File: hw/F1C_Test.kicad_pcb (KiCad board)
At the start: 2 copper layers, 0 parts

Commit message: hw: Partly done layout & routing
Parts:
- added C1: 22u, Capacitor_SMD:C_0603_1608Metric, F.Cu at (116.6, 59.5)
- added C10: 100n, Capacitor_SMD:C_0402_1005Metric, F.Cu at (139.1, 72.3)
- added C11: 100n, Capacitor_SMD:C_0402_1005Metric, F.Cu at (136.3, 74.3)
- added C12: 100n, Capacitor_SMD:C_0402_1005Metric, F.Cu at (132.9, 82.1)
- added C13: 10u, Capacitor_SMD:C_0402_1005Metric, F.Cu at (143.6, 85.6)
- added C14: 100n, Capacitor_SMD:C_0402_1005Metric, F.Cu at (144.3, 84.9)
- added C15: 100n, Capacitor_SMD:C_0402_1005Metric, F.Cu at (139.1, 88.0)
- added C16: 100n, Capacitor_SMD:C_0402_1005Metric, F.Cu at (145.1, 84.1)
- added C17: 100n, Capacitor_SMD:C_0402_1005Metric, F.Cu at (137.0, 73.6)
- added C18: 100n, Capacitor_SMD:C_0402_1005Metric, F.Cu at (134.6, 76.0)
- added C19: 100n, Capacitor_SMD:C_0402_1005Metric, F.Cu at (138.4, 70.0)
- added C2: 22u, Capacitor_SMD:C_0603_1608Metric, F.Cu at (122.6, 59.5)
- added C20: 4.7u, Capacitor_SMD:C_0402_1005Metric, F.Cu at (128.7, 86.2)
- added C21: 4.7u, Capacitor_SMD:C_0402_1005Metric, F.Cu at (128.4, 90.5)
- added C22: 10u, Capacitor_SMD:C_0402_1005Metric, F.Cu at (145.3, 62.6)
- added C23: 100n, Capacitor_SMD:C_0402_1005Metric, F.Cu at (119.5, 53.5)
- added C24: 100n, Capacitor_SMD:C_0402_1005Metric, F.Cu at (119.1, 65.2)
- added C25: 100n, Capacitor_SMD:C_0402_1005Metric, F.Cu at (121.0, 65.2)
- added C3: 22u, Capacitor_SMD:C_0603_1608Metric, F.Cu at (128.6, 59.5)
- added C4: 30p, Capacitor_SMD:C_0402_1005Metric, F.Cu at (150.3, 73.3)
- added C5: 30p, Capacitor_SMD:C_0402_1005Metric, F.Cu at (149.8, 77.6)
- added C6: 10u, Capacitor_SMD:C_0402_1005Metric, F.Cu at (132.1, 80.9)
- added C7: 100n, Capacitor_SMD:C_0402_1005Metric, F.Cu at (133.5, 82.8)
- added C8: 100n, Capacitor_SMD:C_0402_1005Metric, F.Cu at (137.8, 87.0)
- added C9: 100n, Capacitor_SMD:C_0402_1005Metric, F.Cu at (146.5, 77.4)
- added D1: 1N5819, Diode_SMD:D_SOD-323, F.Cu at (124.8, 88.2)
- added D2: White, LED_SMD:LED_0603_1608Metric, F.Cu at (150.6, 81.2)
- added J1: USB_C_Receptacle_USB2.0_14P, Connector_USB:USB_C_Receptacle_HRO_TYPE-C-31-M-12, F.Cu at (140.0, 51.7)
- added J2: FPC/FFC P0.5, FFC_Connector:FPC_1x40_P0.5_L, F.Cu at (140.0, 95.9)
- added J3: 1x03 P2.54, Connector_PinHeader_2.54mm:PinHeader_1x03_P2.54mm_Vertical, F.Cu at (156.4, 85.9)
- added J4: 1x06 P2.54, Connector_PinHeader_2.54mm:PinHeader_1x06_P2.54mm_Vertical, F.Cu at (156.4, 63.8)
- added J5: AudioJack4, Connector_Audio:Jack_3.5mm_KoreanHropartsElec_PJ-320D-4A_Horizontal, F.Cu at (122.7, 73.3)
- added L1: 4.7u, Inductor_SMD:L_Sunlord_SWPA3015S, F.Cu at (119.2, 59.8)
- added L2: 4.7u, Inductor_SMD:L_Sunlord_SWPA3015S, F.Cu at (125.2, 59.8)
- added L3: 2.2u, Inductor_SMD:L_Sunlord_SWPA3015S, F.Cu at (131.2, 59.8)
- added L4: 4.7u, Inductor_SMD:L_Sunlord_SWPA3015S, F.Cu at (125.9, 84.9)
- added R1: 560k, Resistor_SMD:R_0402_1005Metric, F.Cu at (116.8, 57.1)
- added R10: 4.7k, Resistor_SMD:R_0402_1005Metric, F.Cu at (148.2, 81.2)
- added R11: 4.7, Resistor_SMD:R_0402_1005Metric, F.Cu at (119.1, 67.2)
- added R12: 4.7, Resistor_SMD:R_0402_1005Metric, F.Cu at (121.0, 67.2)
- added R13: 5.1k, Resistor_SMD:R_0402_1005Metric, F.Cu at (140.6, 58.4)
- added R14: 5.1k, Resistor_SMD:R_0402_1005Metric, F.Cu at (138.6, 58.4)
- added R15: 100k, Resistor_SMD:R_0402_1005Metric, F.Cu at (153.8, 57.6)
- added R16: 100k, Resistor_SMD:R_0402_1005Metric, F.Cu at (162.4, 57.3)
- added R2: 130k, Resistor_SMD:R_0402_1005Metric, F.Cu at (116.8, 55.2)
- added R3: 110k, Resistor_SMD:R_0402_1005Metric, F.Cu at (122.8, 57.1)
- added R4: 33k, Resistor_SMD:R_0402_1005Metric, F.Cu at (122.8, 55.2)
- added R5: 110k, Resistor_SMD:R_0402_1005Metric, F.Cu at (128.8, 57.1)
- added R6: 130k, Resistor_SMD:R_0402_1005Metric, F.Cu at (128.8, 55.2)
- added R7: 2.2k, Resistor_SMD:R_0402_1005Metric, F.Cu at (145.0, 86.3)
- added R8: 2.2k, Resistor_SMD:R_0402_1005Metric, F.Cu at (146.3, 84.9)
- added R9: 4.7, Resistor_SMD:R_0402_1005Metric, F.Cu at (126.5, 90.5)
- added SW1: SW_Push, Button_Switch_SMD:SW_Push_1TS009xxxx-xxxx-xxxx_6x6x5mm, F.Cu at (153.2, 52.5)
- added SW2: SW_Push, Button_Switch_SMD:SW_Push_1TS009xxxx-xxxx-xxxx_6x6x5mm, F.Cu at (162.2, 52.3)
- added SW3: SW_SPST, Switches:SPST_1x01_P2.54, F.Cu at (140.1, 61.2)
- added U1: ME3103, Package_TO_SOT_SMD:SOT-23-5, F.Cu at (119.0, 56.0)
- added U2: ME3103, Package_TO_SOT_SMD:SOT-23-5, F.Cu at (125.0, 56.0)
- added U3: ME3103, Package_TO_SOT_SMD:SOT-23-5, F.Cu at (131.0, 56.0)
- added U4: F1C100s, F1C100s:QFN40P1000X1000X90-89N-D, F.Cu at (140.0, 80.0)
- added U5: W25Q32JVSS, Package_SO:SOIC-8_5.3x5.3mm_P1.27mm, F.Cu at (143.2, 70.0)
- added U6: MT9284, Package_TO_SOT_SMD:SOT-23-6, F.Cu at (127.8, 88.3)
- added Y1: 24MHz 20pF, Crystal:Crystal_SMD_3225-4Pin_3.2x2.5mm, F.Cu at (148.8, 75.5)
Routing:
- net /PWR: track 0.00 -> 29.1 mm
- net /LCD_VSYNC: track 0.00 -> 28.1 mm, vias 0 -> 2
- net /LCD_DE: track 0.00 -> 25.7 mm, vias 0 -> 2
- net /LCD_HSYNC: track 0.00 -> 25.3 mm, vias 0 -> 2
- net /LCD_PCLK: track 0.00 -> 24.6 mm, vias 0 -> 2
- net /JTAG_TCK: track 0.00 -> 16.3 mm
- net /LCD_D2: track 0.00 -> 15.9 mm
- net /LCD_D3: track 0.00 -> 15.7 mm
- net /LCD_D4: track 0.00 -> 15.6 mm
- net /LCD_D5: track 0.00 -> 15.4 mm
- net /LCD_D6: track 0.00 -> 15.3 mm
- net /LCD_D7: track 0.00 -> 15.1 mm
- net /LCD_D10: track 0.00 -> 14.9 mm
- net /LCD_D11: track 0.00 -> 14.8 mm
- net /LCD_D12: track 0.00 -> 14.6 mm
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- added copper zone on B.Cu, net GND
- added copper zone on F.Cu, net GND

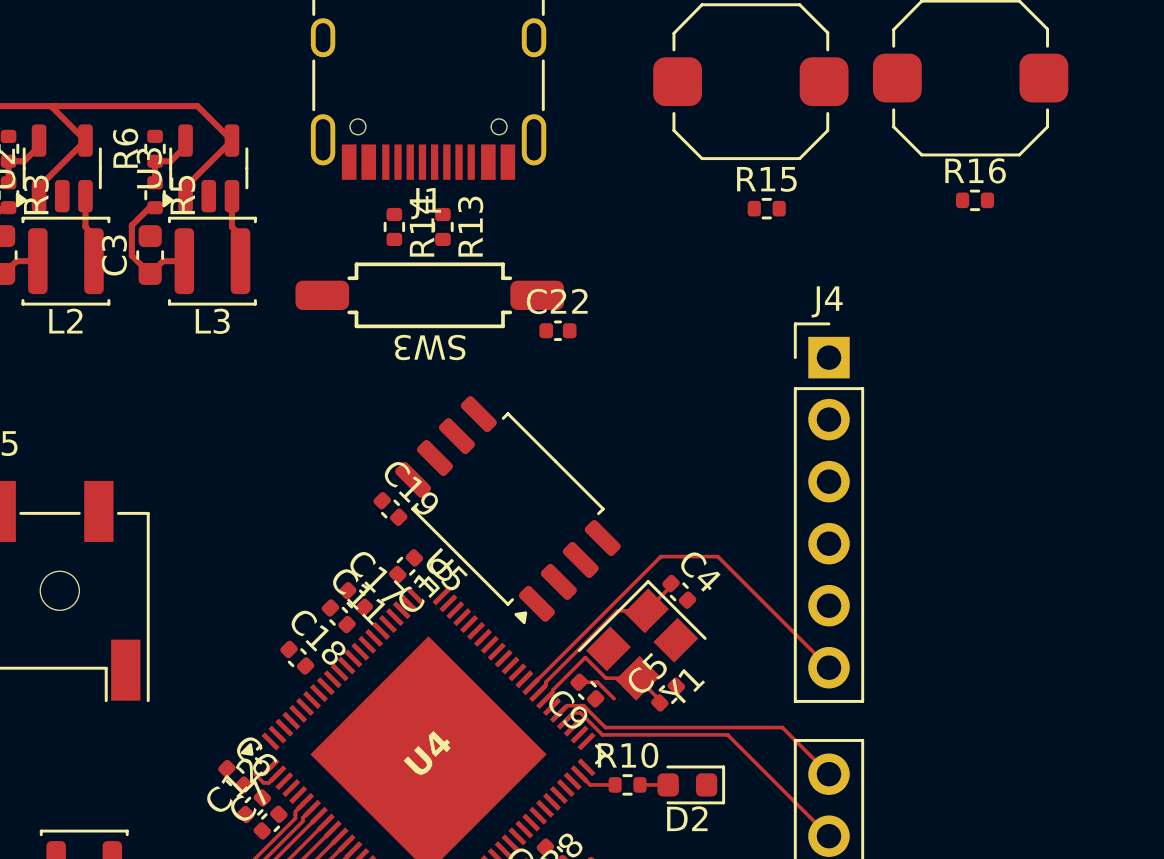
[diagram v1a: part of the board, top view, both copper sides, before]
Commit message: hw: Add VRA decoupling networks
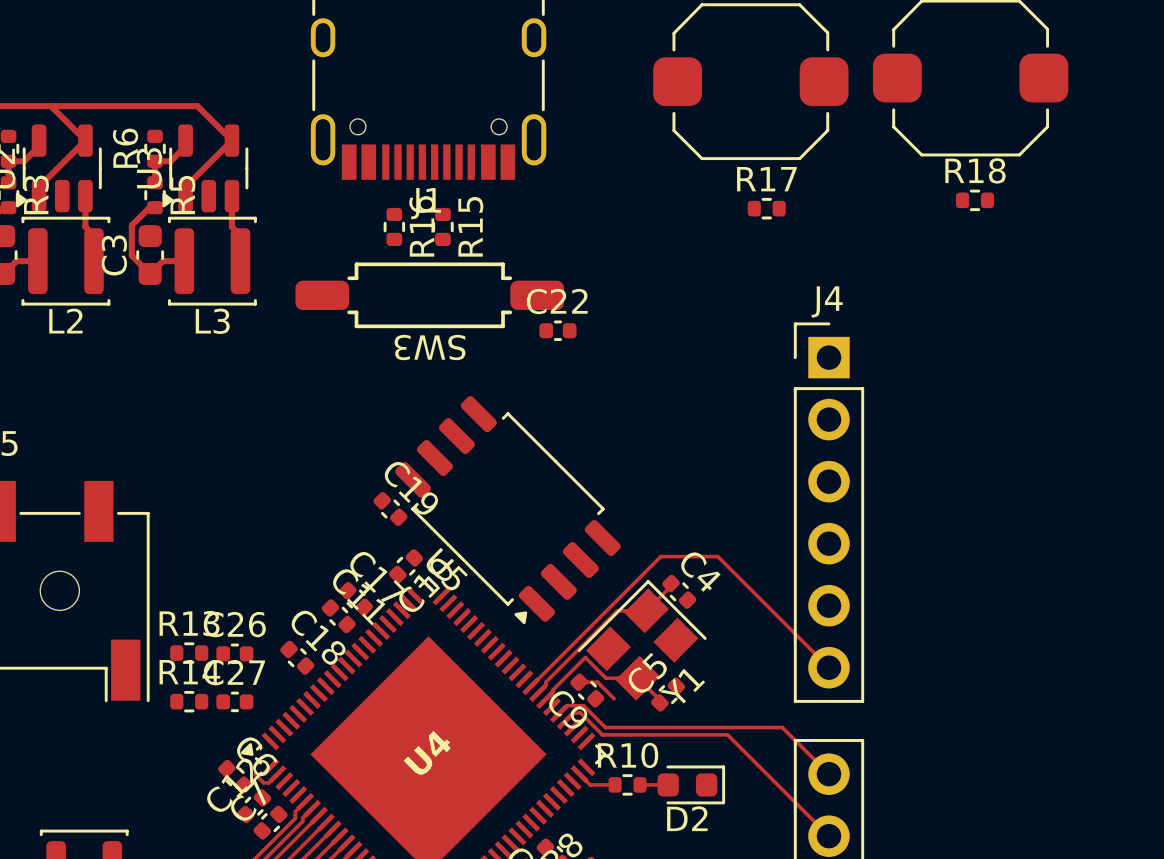
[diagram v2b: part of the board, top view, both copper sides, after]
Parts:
- added C26: 1u, Capacitor_SMD:C_0402_1005Metric, F.Cu at (132.1, 75.9)
- added C27: 1u, Capacitor_SMD:C_0402_1005Metric, F.Cu at (132.1, 77.8)
- added R13: 200k, Resistor_SMD:R_0402_1005Metric, F.Cu at (130.2, 75.8)
- added R14: 200k, Resistor_SMD:R_0402_1005Metric, F.Cu at (130.2, 77.8)
- renumbered R13 to R15, R14 to R16, R15 to R17, R16 to R18
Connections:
- U4 pad 81: unconnected-(U4A-VRA1-Pad81) -> /VRA1
- U4 pad 83: unconnected-(U4A-VRA2-Pad83) -> /VRA2

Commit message: hw: Further incomplete revisions...
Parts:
- J2: footprint FFC_Connector:FPC_1x40_P0.5_L -> FFC_Connector:FPC_1x40_P0.5_R
- moved D1 25.4 mm to (150.1, 90.2)
- moved R9 25.4 mm to (151.8, 92.5)
- moved U6 25.4 mm to (153.1, 90.3)
- moved C20 25.4 mm to (153.9, 88.1)
- moved C21 25.4 mm to (153.7, 92.5)
- moved L4 25.4 mm to (151.2, 86.8)
- moved C19 0.83 mm to (137.7, 69.6)
- moved U5 0.83 mm to (142.5, 69.6)
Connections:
- U4 pad 38: /LCD_NRST -> unconnected-(U4A-PE11/CLK_OUT/TWI0_SCK/IR_RX/EINTE11-Pad38)
- U4 pad 45: unconnected-(U4A-PE4/CSI_D1/LCD_D16/DA_LRCK/RSB_SDA/EINTE4-Pad45) -> /LCD_NRST
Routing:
- net /LCD_VSYNC: track 28.1 -> 6.73 mm, vias 2 -> 0
- net /LCD_DE: track 25.7 -> 6.72 mm, vias 2 -> 0
- net /LCD_HSYNC: track 25.3 -> 6.62 mm, vias 2 -> 0
- net /LCD_LED_DIM: track 0.00 -> 18.0 mm, vias 0 -> 2
- net /LCD_CS: track 0.00 -> 16.9 mm, vias 0 -> 2
- net /JTAG_TMS: track 0.00 -> 16.5 mm
- net /LCD_NRST: track 0.00 -> 16.3 mm
- net /JTAG_TDI: track 0.00 -> 16.0 mm
- net /JTAG_TDO: track 0.00 -> 15.8 mm
- net /LCD_MOSI: track 0.00 -> 14.7 mm
- net /LCD_PCLK: track 24.6 -> 9.87 mm, vias 2 -> 0
- net /LCD_SCLK: track 0.00 -> 14.5 mm
- net /FLASH_CLK: track 0.00 -> 12.7 mm
- net /FLASH_MOSI: track 0.00 -> 11.8 mm
- net /LCD_D19: track 13.9 -> 3.42 mm
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
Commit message: hw: Layout & routing (WIP)
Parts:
- moved R2 17.8 mm to (131.9, 45.8), turned to 0 degrees
- moved C1 17.8 mm to (127.5, 45.5), turned to 0 degrees
- moved R1 17.4 mm to (130.0, 45.8), turned to 180 degrees
- moved U1 14.5 mm to (131.1, 48.0), turned to 0 degrees
- moved L1 14.3 mm to (127.3, 48.1), turned to 90 degrees
- moved C23 14.0 mm to (133.2, 56.5)
- moved R18 13.7 mm to (149.4, 52.9)
- moved C24 13.2 mm to (127.0, 75.8), turned to 180 degrees
- moved R11 13.0 mm to (128.9, 75.8), turned to 180 degrees
- moved R17 11.8 mm to (146.1, 66.5)
- moved SW1 11.3 mm to (148.3, 62.7), turned to 90 degrees
- moved SW2 11.0 mm to (151.7, 49.0), turned to 90 degrees
- moved C25 10.4 mm to (127.0, 73.8), turned to 180 degrees
- moved R12 10.2 mm to (128.9, 73.8), turned to 180 degrees
- moved J5 9.92 mm to (130.7, 67.5)
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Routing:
- net /USB_D+: track 0.00 -> 23.9 mm
- net /USB_D-: track 0.00 -> 23.7 mm
- net /HP_COM: track 1.21 -> 21.9 mm
- net /LCD_D21: track 2.64 -> 18.2 mm, vias 0 -> 2
- net /LCD_D22: track 2.83 -> 18.3 mm, vias 0 -> 2
- net Net-(C24-Pad1): track 0.00 -> 15.4 mm
- net /LCD_D20: track 2.66 -> 16.2 mm, vias 0 -> 2
- net /LCD_D18: track 3.76 -> 16.6 mm, vias 0 -> 2
- net /LCD_D19: track 3.42 -> 16.2 mm, vias 0 -> 2
- net /LCD_D15: track 4.14 -> 16.9 mm, vias 0 -> 2
- net /LCD_D14: track 4.56 -> 17.3 mm, vias 0 -> 2
- net /LCD_D13: track 4.97 -> 17.6 mm, vias 0 -> 2
- net /LCD_D12: track 5.39 -> 17.9 mm, vias 0 -> 2
- net /LCD_D11: track 5.80 -> 18.2 mm, vias 0 -> 2
- net /LCD_D10: track 6.22 -> 18.6 mm, vias 0 -> 2
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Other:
- board outline added: 32 x 56 mm

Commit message: hw: More routing
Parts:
- moved C22 4.00 mm to (144.2, 55.6)
- moved R18 1.20 mm to (148.2, 52.9)
- moved SW2 1.20 mm to (150.5, 49.0)
- moved R16 0.35 mm to (138.1, 54.4)
- moved C15 0.30 mm to (138.8, 88.1), turned to 45 degrees
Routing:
- net +3V3: track 6.88 -> 94.4 mm, vias 0 -> 6
- net /PWR: track 30.6 -> 89.9 mm, vias 0 -> 2
- net +2V6: track 5.17 -> 46.6 mm, vias 0 -> 2
- net +1V1: track 5.17 -> 36.5 mm, vias 0 -> 2
- net /FLASH_CS: track 2.35 -> 28.8 mm, vias 0 -> 2
- net VBUS: track 0.00 -> 23.3 mm, vias 0 -> 2
- net /~{RESET}: track 0.00 -> 23.0 mm, vias 0 -> 2
- net Net-(U4B-SVREF): track 0.00 -> 4.01 mm
- net /USB_D+: track 23.9 -> 26.8 mm
- net /USB_D-: track 23.7 -> 26.0 mm, vias 0 -> 2
- net Net-(J1-CC2): track 0.00 -> 1.73 mm
- net Net-(J1-CC1): track 0.00 -> 1.73 mm
- net /LCD_D23: track 13.1 -> 12.6 mm
- net /LCD_D22: track 18.3 -> 17.8 mm
- net GND: vias 6 -> 15

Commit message: hw: Finish routing, finally
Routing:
- net +3V3: track 94.4 -> 143.5 mm, vias 6 -> 8
- net +1V1: track 36.5 -> 65.4 mm, vias 2 -> 5
- net +2V6: track 46.6 -> 65.0 mm, vias 2 -> 5

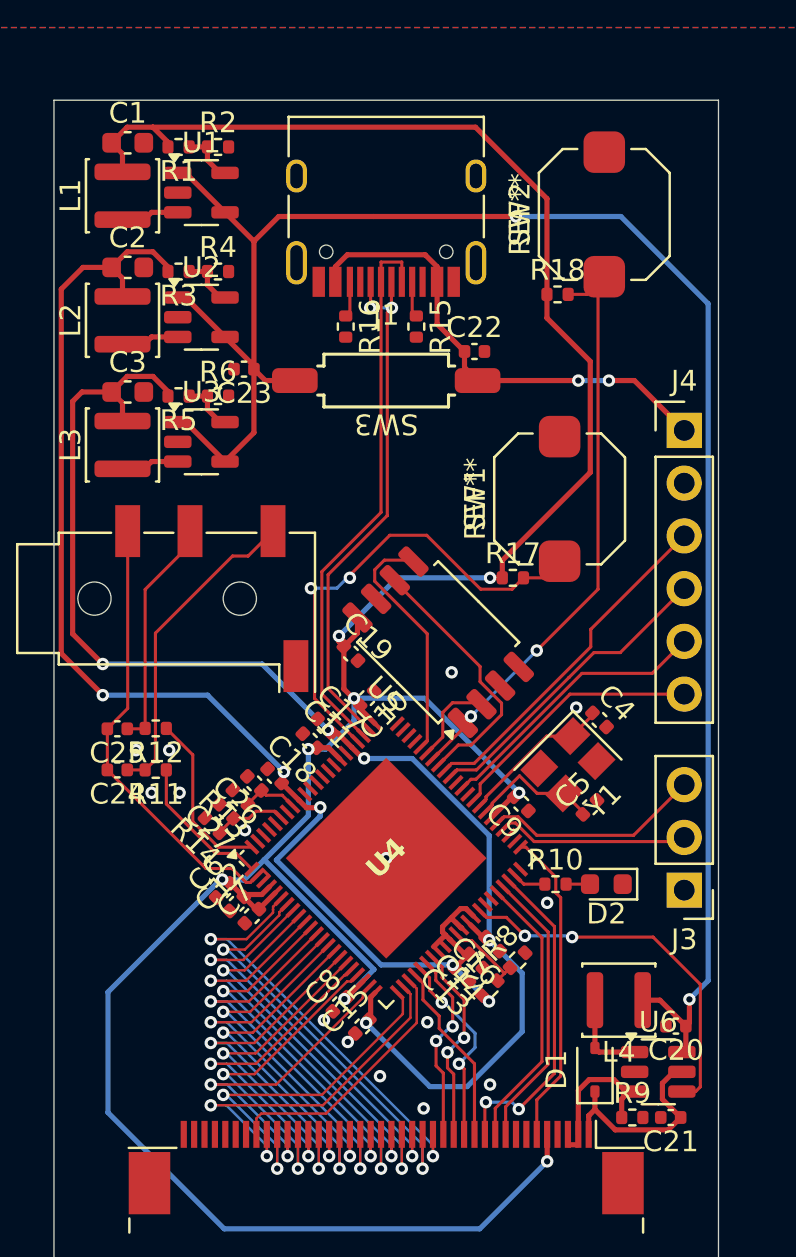
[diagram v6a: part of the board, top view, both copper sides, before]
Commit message: hw: Fine-tune tracks, adapting to round-tracks plug-in
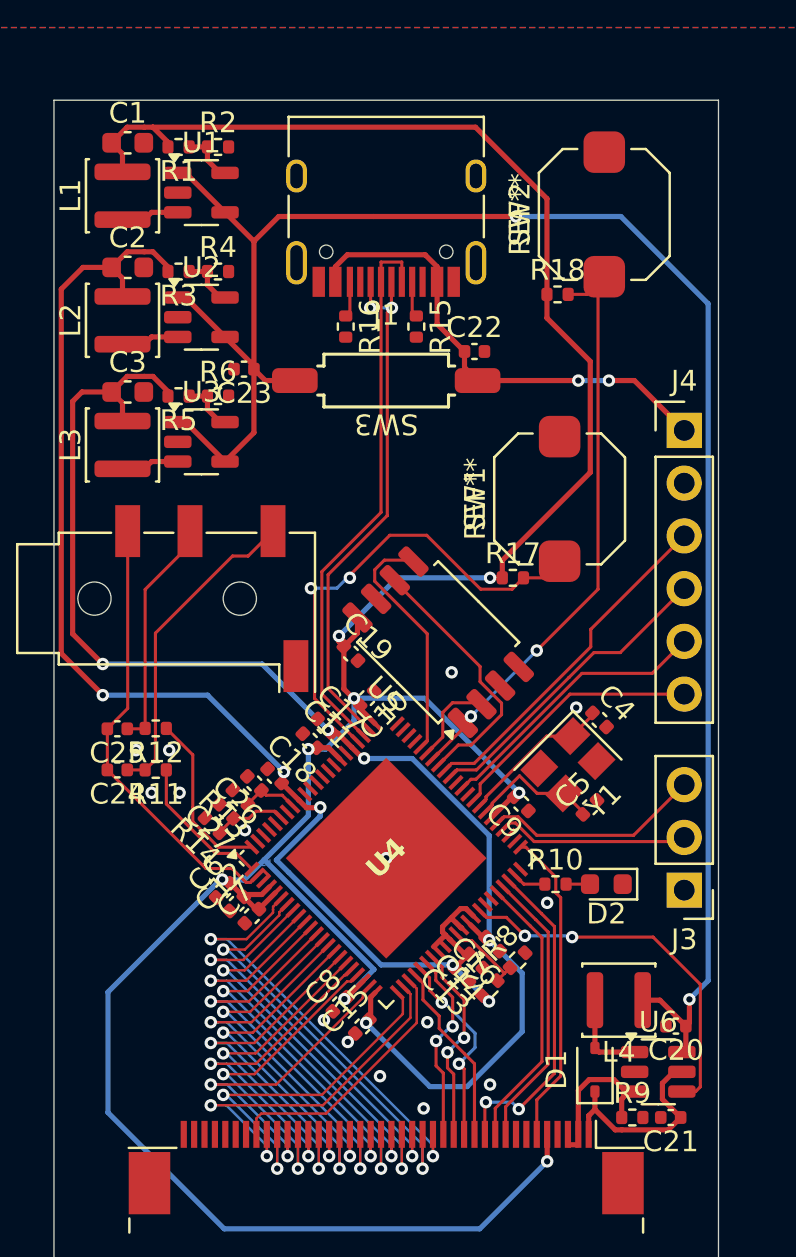
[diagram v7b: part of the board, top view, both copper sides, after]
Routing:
- added copper zone on B.Cu, net +3V3

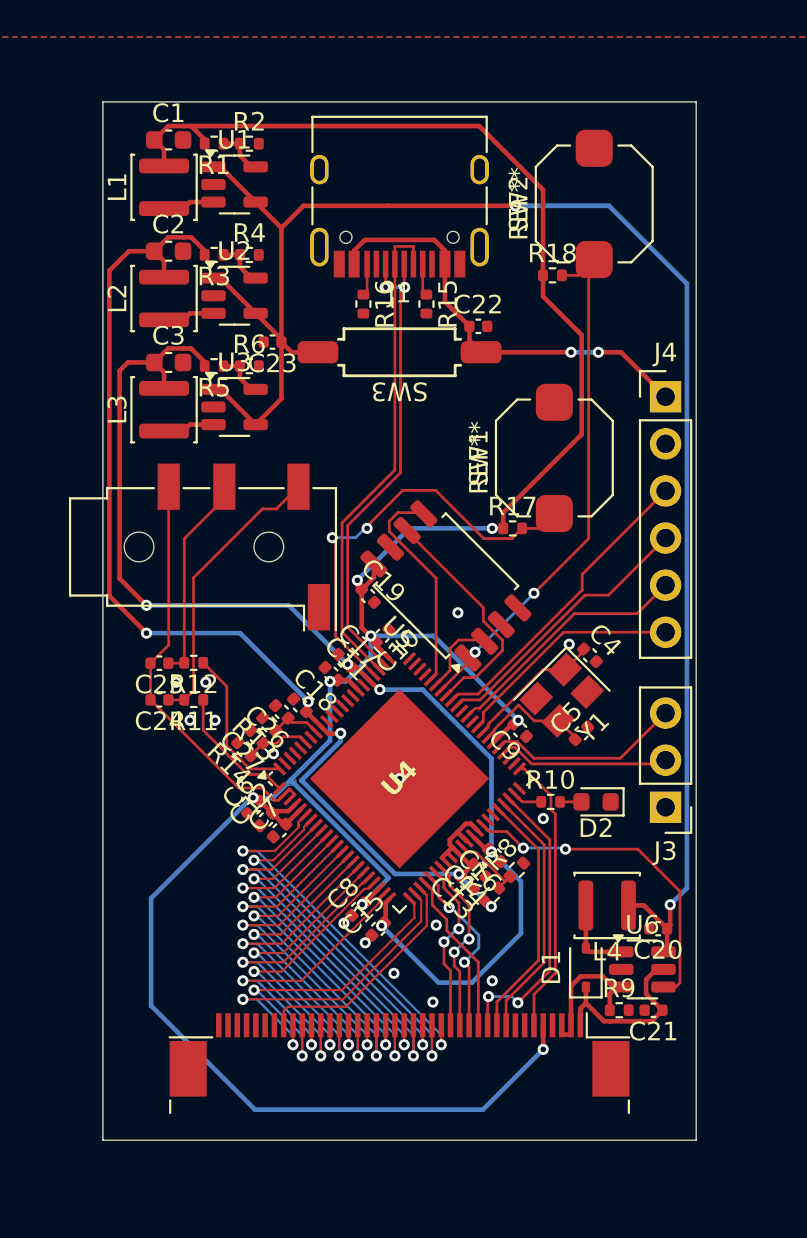
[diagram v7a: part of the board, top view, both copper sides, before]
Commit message: hw: Add a lot of stitching holes
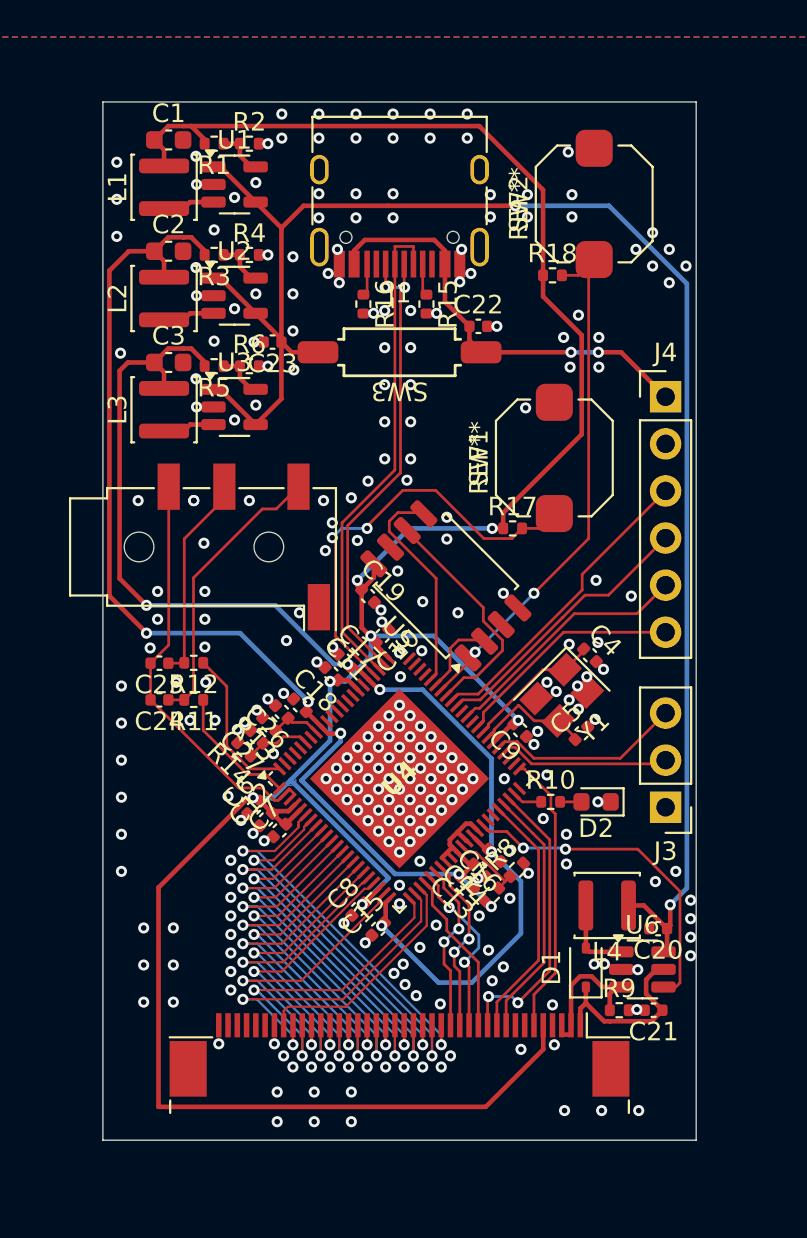
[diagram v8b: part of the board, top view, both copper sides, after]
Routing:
- net +3V3: track 143.5 -> 146.2 mm, vias 8 -> 7
- net GND: vias 15 -> 288
